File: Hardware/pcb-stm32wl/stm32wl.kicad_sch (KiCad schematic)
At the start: 27 parts, among them J1 USB_C_Receptacle_USB2.0_16P, U1 NUCLEO-L476RG, U2 MCP73831/2, U4 TPS22910AYZVR, U5 STM32WL55CCU6, X2 32MHz, Y1 32.768KHz

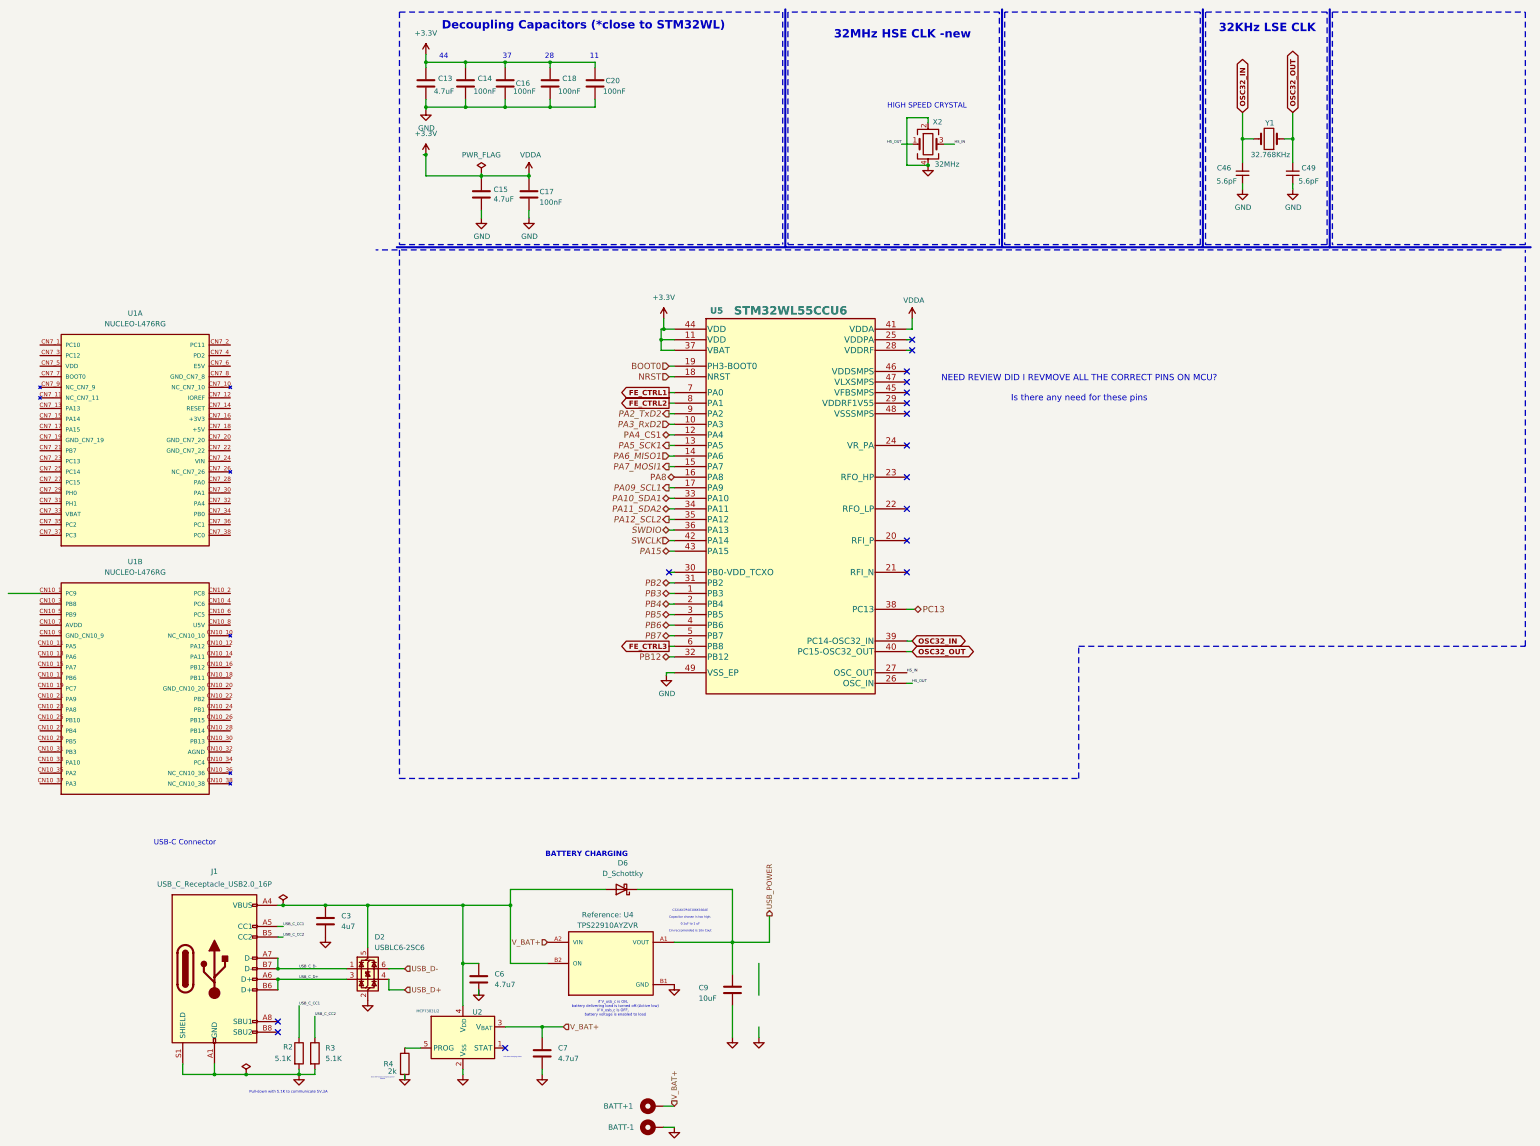
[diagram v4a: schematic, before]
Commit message: . Added NUCLEO reference schematics . Cleaned, renamed schematic pins for clarity . Fixed PMOS polarity bug . Added PMOS for switching StrainV . Added capacitors to AIN, StrainV . Cleaned git repository by removing backups, temporary lck files, ignoring KiCad cache files
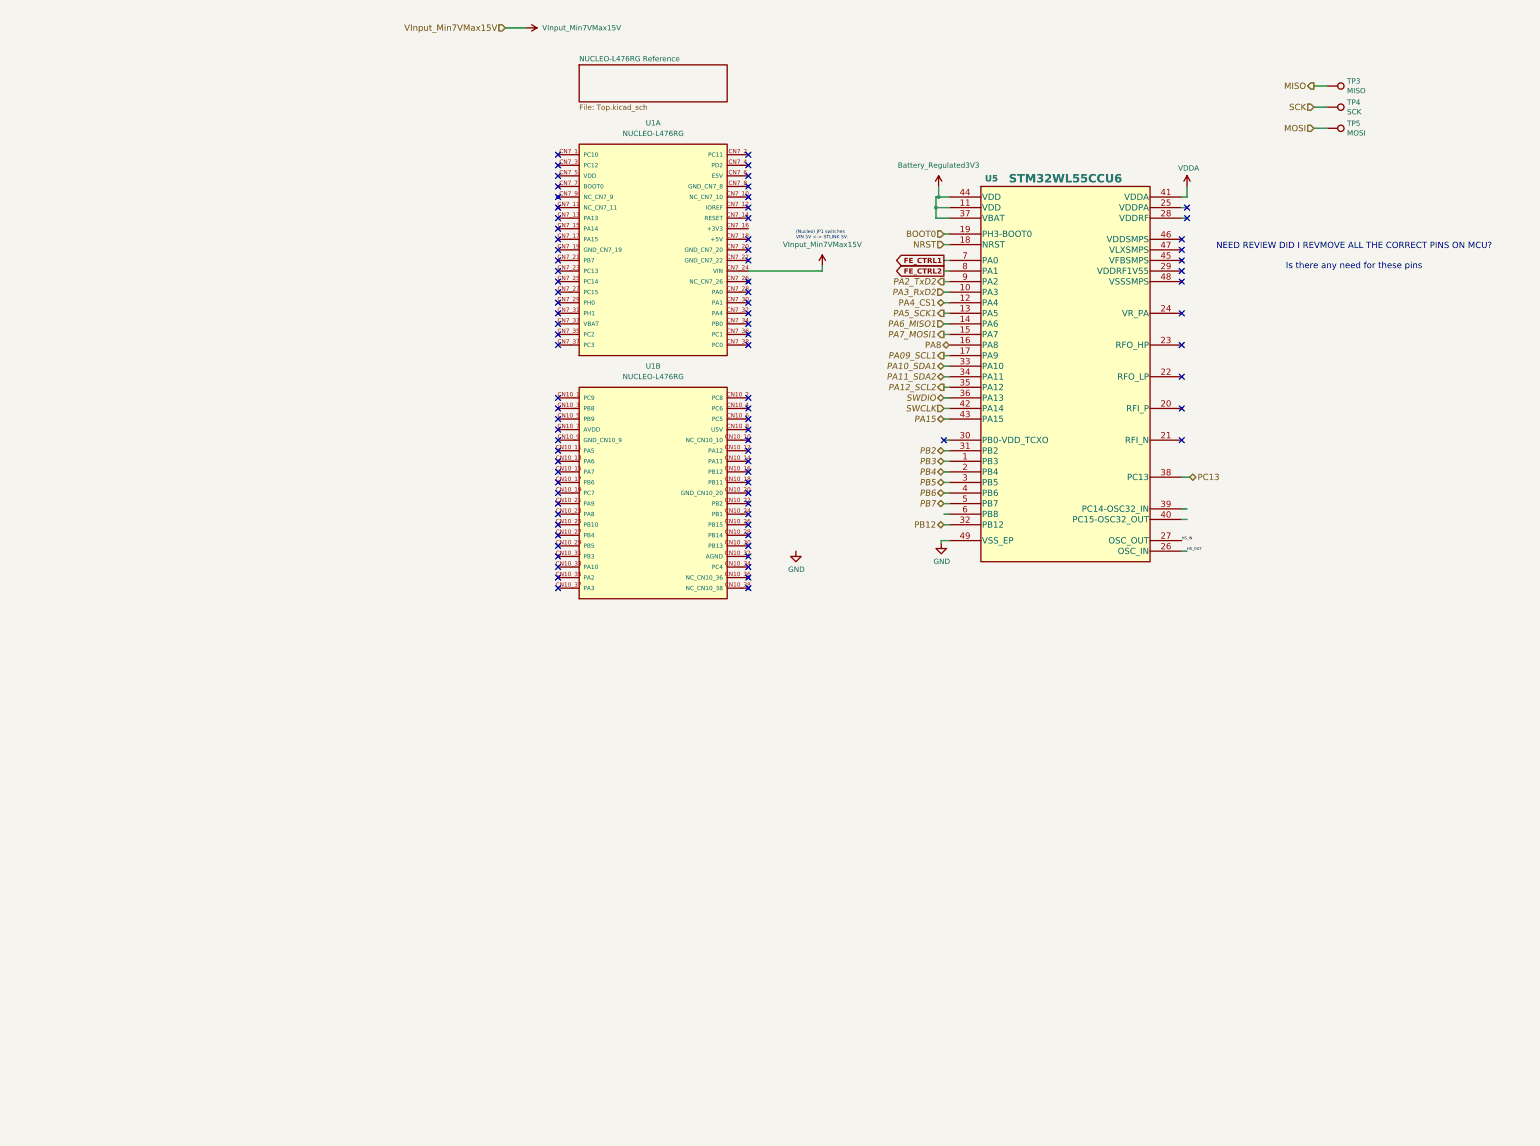
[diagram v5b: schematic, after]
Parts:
- removed BATT+1, BATT-1: MountingHole_Pad, MountingHole:MountingHole_2.2mm_M2_Pad, symbol Mechanical:MountingHole_Pad
- removed C13, C15: 4.7uF, Capacitor_SMD:C_0603_1608Metric, symbol Device:C
- removed C14, C16, C17, C18, C20: 100nF, Capacitor_SMD:C_0402_1005Metric, symbol Device:C
- removed C3: 4u7, Capacitor_SMD:C_0603_1608Metric, symbol Device:C
- removed C46, C49: 5.6pF, Capacitor_SMD:C_0402_1005Metric, symbol Device:C_Small
- removed C6, C7: 4.7u7, Capacitor_SMD:C_0603_1608Metric, symbol Device:C
- removed C9: 10uF, Capacitor_SMD:C_1206_3216Metric, symbol Device:C
- removed D2: USBLC6-2SC6, Package_TO_SOT_SMD:SOT-23-6, symbol Power_Protection:USBLC6-2SC6
- removed D6: D_Schottky, Diode_SMD:D_SOD-323F, symbol Device:D_Schottky
- removed J1: USB_C_Receptacle_USB2.0_16P, Connector_USB:USB_C_Receptacle_GCT_USB4105-xx-A_16P_TopMnt_Horizontal, symbol Connector:USB_C_Receptacle_USB2.0_16P
- removed R2, R3: 5.1K, Resistor_SMD:R_0603_1608Metric, symbol Device:R
- removed R4: 2k, Resistor_SMD:R_0603_1608Metric, symbol Device:R
- removed U2: MCP73831/2, Package_TO_SOT_SMD:SOT-23-5, symbol Battery_Management:MCP73831-2-OT
- removed U4: TPS22910AYZVR, TPS22910A:BGA4N50P2X2_88X88X50N, symbol TPS22910AYZVR:TPS22910AYZVR
- removed X2: 32MHz, NX2016SA-32M-EXS00A-CS06465:NX2016SA32MEXS00ACS06465, symbol Device:Crystal_GND24
- removed Y1: 32.768KHz, node-lib-v1:Crystal_SMD_NX2012SA_32.768KHz, symbol Device:Crystal
- added TP3: MISO, TestPoint:TestPoint_Pad_D1.5mm, symbol Connector:TestPoint
- added TP4: SCK, TestPoint:TestPoint_Pad_D1.5mm, symbol Connector:TestPoint
- added TP5: MOSI, TestPoint:TestPoint_Pad_D1.5mm, symbol Connector:TestPoint
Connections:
- net VInput_Min7VMax15V: now reaches U1.CN7_24 (VIN)
- net +3.3V renamed Battery_Regulated3V3
- net Battery_Regulated3V3: no longer U5.41 (VDDA)
- net FE_CTRL3: no longer names the net of U5.6 (PB8)
- net OSC32_IN: no longer names the net of U5.39 (PC14-OSC32_IN)
- net OSC32_OUT: no longer names the net of U5.40 (PC15-OSC32_OUT)
- new net MISO: TP3.1
- new net MOSI: TP5.1
- new net SCK: TP4.1
- new net VDDA: U5.41 (VDDA)
- no-connect marks 16 -> 87
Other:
- added sheet NUCLEO-L476RG Reference (Top.kicad_sch)
- note added: "(Nucleo) JP1 switches VIN 5V <-> STLINK 5V."
- note removed: "11"
- note removed: "28"
- note removed: "2K is the fastest charging speed 500mA"
- note removed: "32KHz LSE CLK"
- note removed: "32MHz HSE CLK -new"
- note removed: "37"
- note removed: "44"
- note removed: "BATTERY CHARGING"
- note removed: "C3216X7R1E106K160AE Capacitor chosen is too high. 0.1uF to 1 uF Cin reccomended is 10x Cout"
- note removed: "Decoupling Capacitors (*close to STM32WL)"
- note removed: "HIGH SPEED CRYSTAL"
- note removed: "Indicates charging status"
- note removed: "Pull-down with 5.1K to communicate 5V,3A"
- note removed: "USB-C Connector"
- note removed: "if V_usb_c is ON, battery delivering load is turned off.(Active low) if V_usb_c is OFF, battery voltage is enabled to load"
- moved on the sheet: U1A, U1B, U5

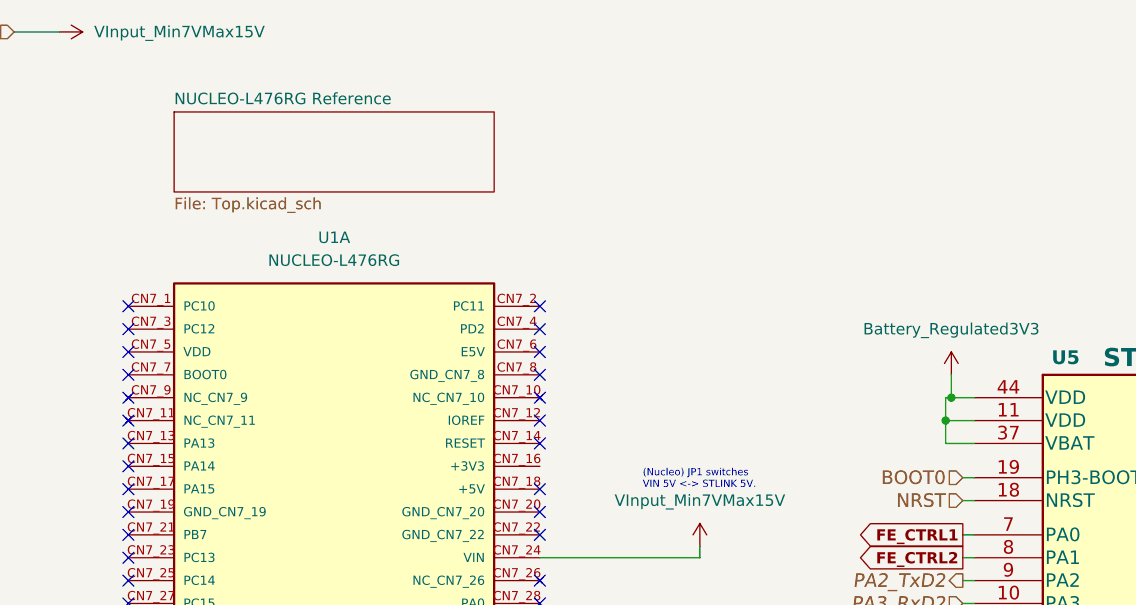
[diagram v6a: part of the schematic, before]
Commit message: . Re-imported NUCLEO_L476RG/BoardDesign/* files using KiCad 9.0.0 one at a time (to avoid a bug evident in misconnections in MCU_64), copied the schematic contents into local kicad_sch files with the same names, prefixed with NUCLEO_L476RG_*
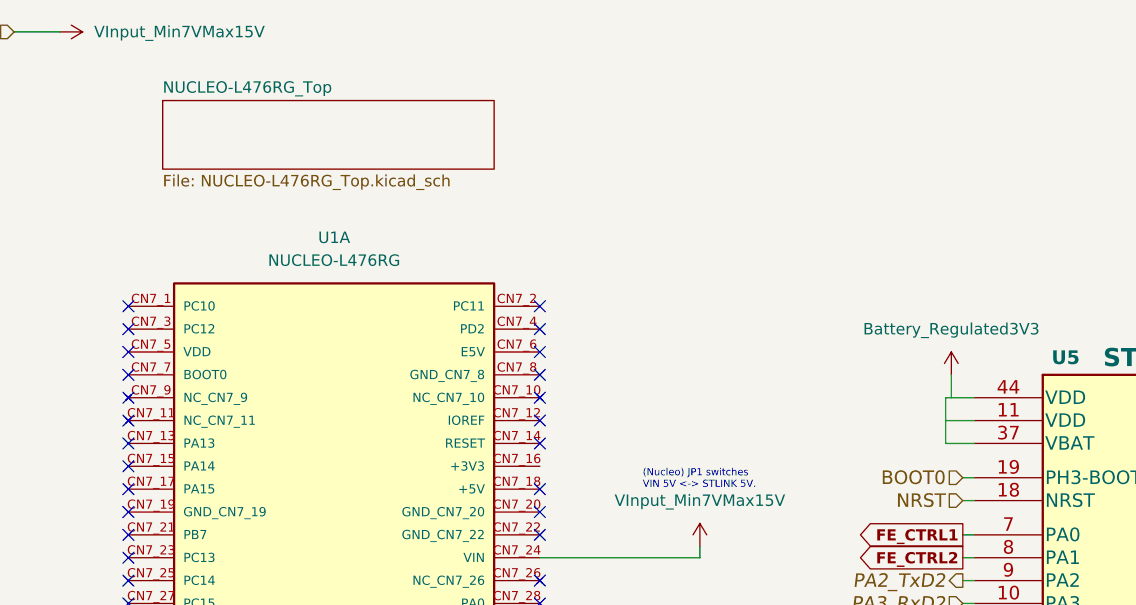
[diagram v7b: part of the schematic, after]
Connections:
- net Battery_Regulated3V3: no longer U5.11 (VDD), U5.37 (VBAT), U5.44 (VDD)
- new net: U5.37 (VBAT), U5.44 (VDD)
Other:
- removed sheet NUCLEO-L476RG Reference
- added sheet NUCLEO-L476RG_Top (NUCLEO-L476RG_Top.kicad_sch)
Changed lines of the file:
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@@
 		)
-	)
-	(junction
-		(at 141.605 59.69)
-		(diameter 0)
-		(color 0 0 0 0)
-	)
-	(junction
-		(at 142.24 57.15)
-		(diameter 0)
-		(color 0 0 0 0)
 	)
 	(no_connect
@@
 	(wire
 		(pts
-			(xy 141.605 62.23) (xy 141.605 59.69)
+			(xy 141.605 57.15) (xy 141.605 62.23)
 		)
 		(stroke
@@
 	(wire
 		(pts
-			(xy 141.605 57.15) (xy 142.24 57.15)
+			(xy 141.605 57.15) (xy 144.78 57.15)
 		)
 		(stroke
@@
 	(wire
 		(pts
-			(xy 141.605 57.15) (xy 141.605 59.69)
-		)
-		(stroke
-			(width 0)
-			(type default)
-		)
-	)
-	(wire
-		(pts
 			(xy 144.78 139.7) (xy 142.875 139.7)
-		)
-		(stroke
-			(width 0)
-			(type default)
-		)
-	)
-	(wire
-		(pts
-			(xy 142.24 57.15) (xy 144.78 57.15)
 		)
 		(stroke
@@
 	)
 	(sheet
-		(at 55.88 25.4)
-		(size 35.56 8.89)
-		(exclude_from_sim no)
-		(in_bom yes)
-		(on_board yes)
+		(at 54.61 24.13)
+		(size 36.83 7.62)
+		(exclude_from_sim yes)
+		(in_bom no)
+		(on_board no)
 		(dnp no)
 		(fields_autoplaced yes)
 		(stroke
-			(width 0)
+			(width 0.1524)
 			(type solid)
-			(color 128 0 0 1)
 		)
 		(fill
-			(color 128 255 128 1.0000)
-		)
-		(property "Sheetname" "NUCLEO-L476RG Reference"
-			(at 55.88 24.6884 0)
+			(color 0 0 0 0.0000)
+		)
+		(property "Sheetname" "NUCLEO-L476RG_Top"
+			(at 54.61 23.4184 0)
 			(effects
 				(font
@@
 			)
 		)
-		(property "Sheetfile" "Top.kicad_sch"
-			(at 55.88 34.8746 0)
-			(effects
-				(font
+		(property "Sheetfile" "NUCLEO-L476RG_Top.kicad_sch"
+			(at 54.61 32.3346 0)
+			(effects
+				(font
